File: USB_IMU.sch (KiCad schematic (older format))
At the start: 12 parts, among them U1301 LSM9DS1, U801 MCIMX7D7DVM10SC

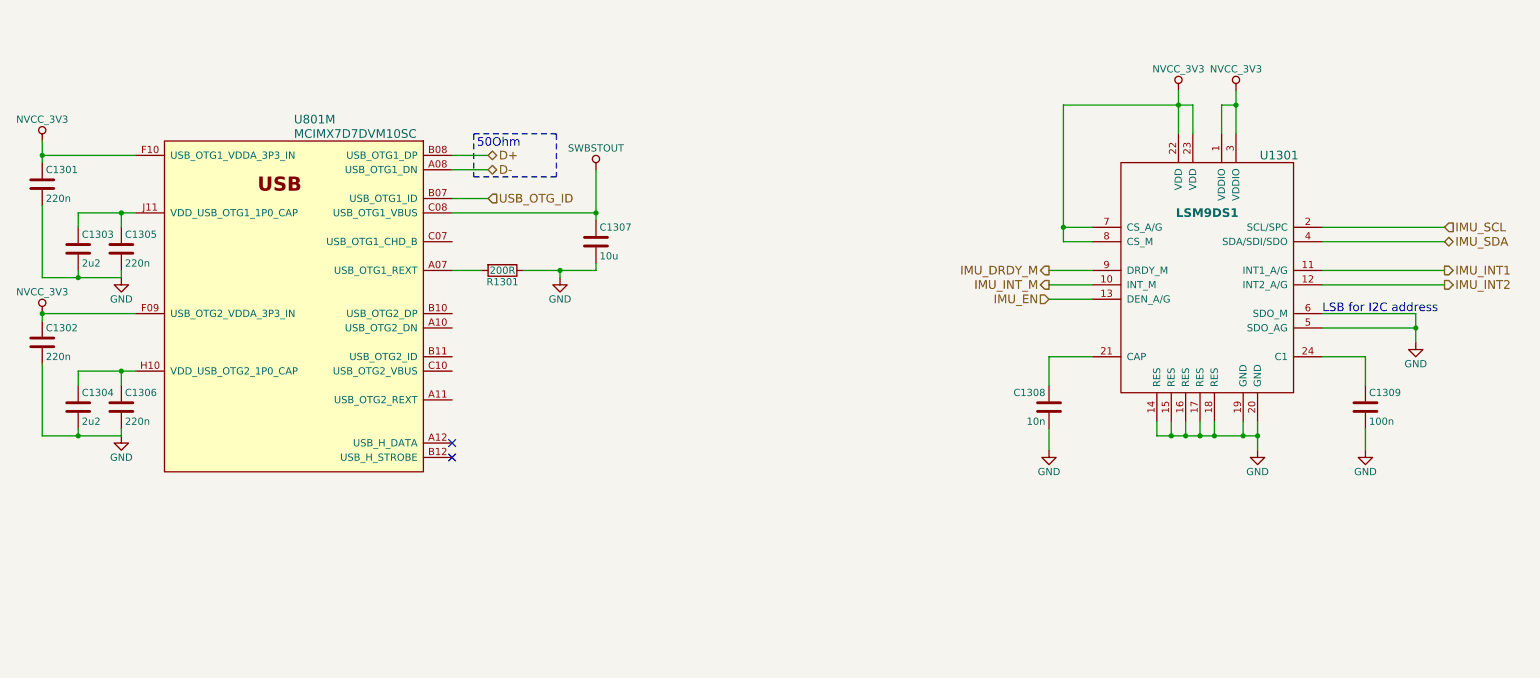
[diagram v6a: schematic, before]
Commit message: This branch moves from i.mx7 to STM32F4 CPU to be finished for Hackaday Prize 2017
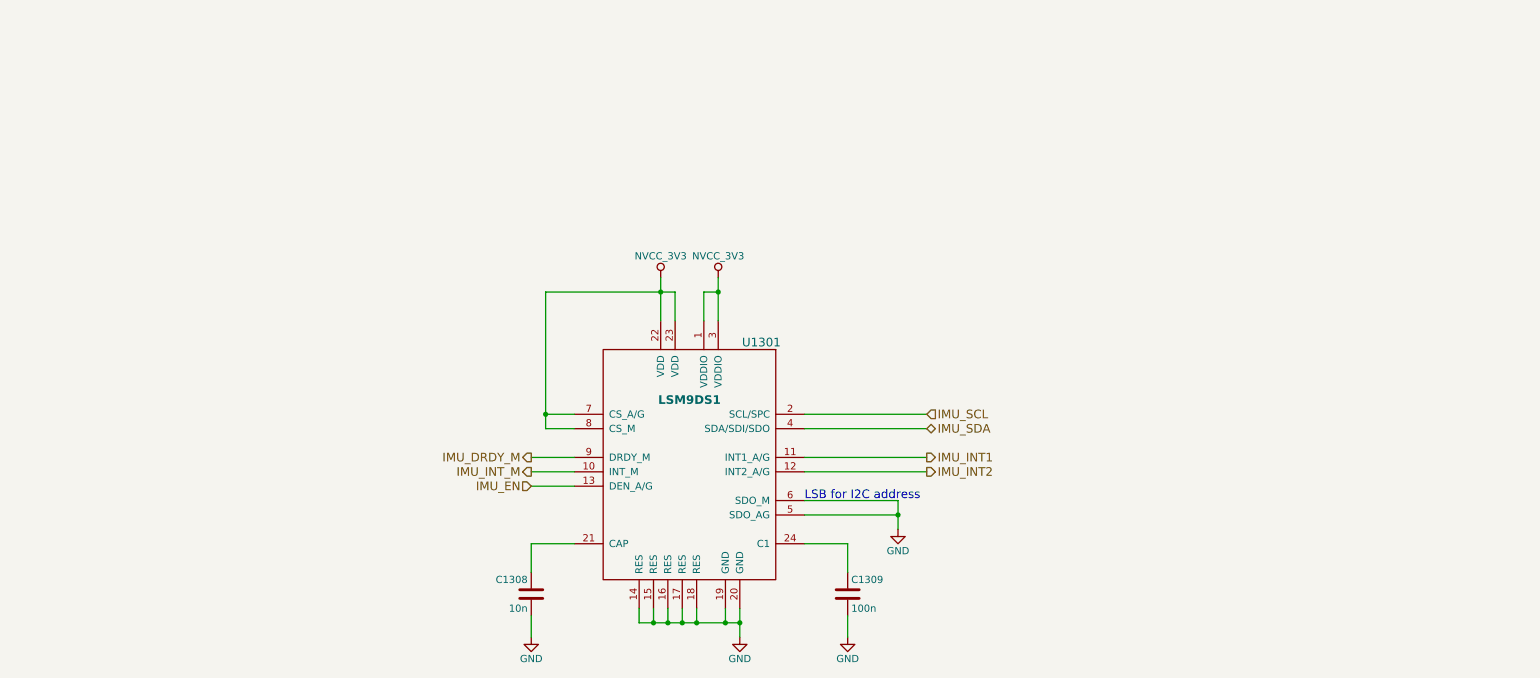
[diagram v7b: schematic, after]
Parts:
- removed C1301, C1302, C1305, C1306: 220n, Capacitors_SMD:C_0402, symbol C
- removed C1303, C1304: 2u2, Capacitors_SMD:C_0603, symbol C
- removed C1307: 10u, Capacitors_SMD:C_0603, symbol C
- removed R1301: 200R, Resistors_SMD:R_0402, symbol R
- removed U801: MCIMX7D7DVM10SC, NokiaRetroFit:BGA_541_075_19x19, symbol MCIMX7D7DVM10SC
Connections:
- no-connect marks 2 -> 0
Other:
- note removed: "50Ohm"
- moved on the sheet: C1308, C1309, U1301

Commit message: Modification for STM32 adaption
For the Hackaday Prize 2017 I decided to switch to STM32 as CPU

*Power system was modified to just contain the charge IC,
*Boost converter for high voltage peripherals
*Buck converter for 3V3 for CPU and switchable NVCC_3V3
   for peripherie

CPU signals are routed and pinmux is done in firmware folder.

SD-Card has 4bit Interface

WiFi module ESP8266 is connected via UART

Wolfson Ausio codec is connected via SAI

Two digital microphones for noise canceling

Rumble Motor driver

LCD is connected via it's own I2C interface
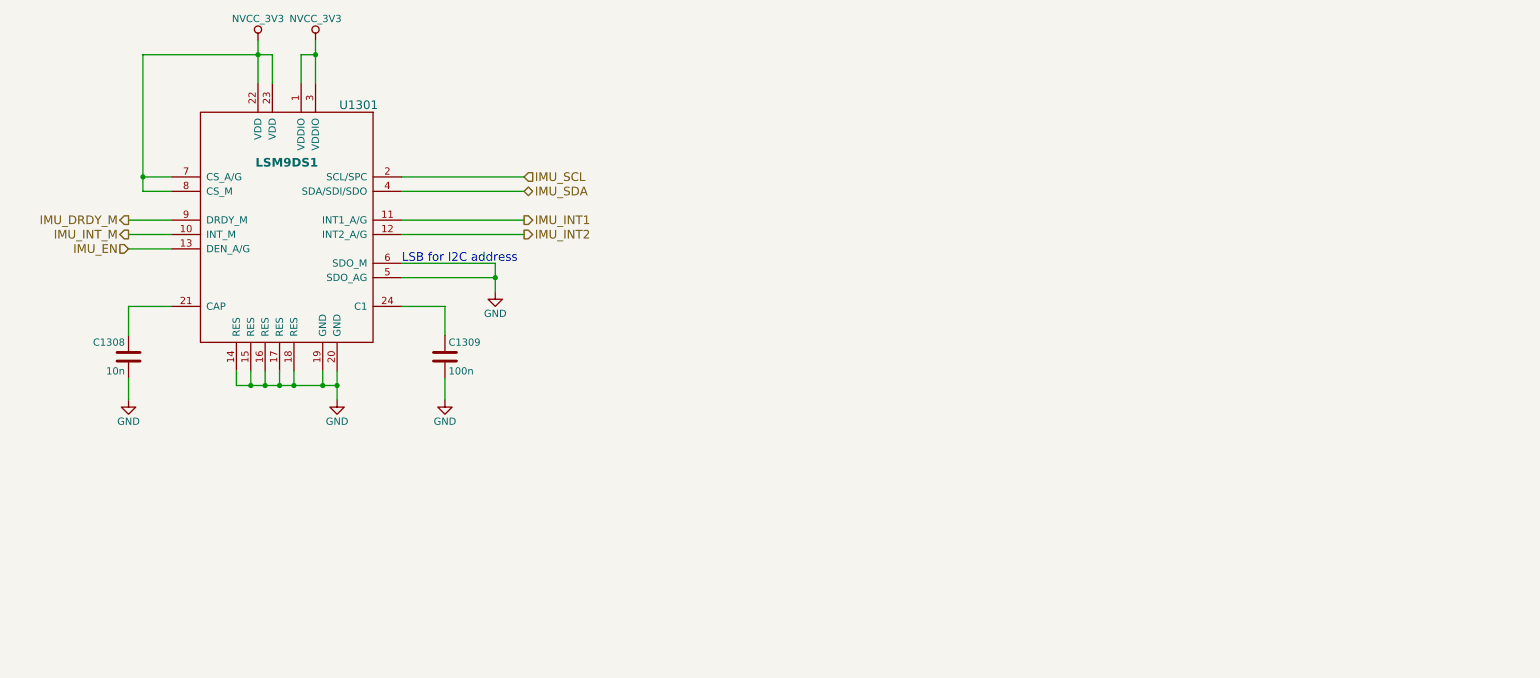
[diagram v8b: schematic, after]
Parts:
- C1308: footprint Capacitors_SMD:C_0603 -> Capacitors_SMD:C_0402_NoSilk
- C1309: footprint Capacitors_SMD:C_0402 -> Capacitors_SMD:C_0402_NoSilk
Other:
- moved on the sheet: C1308, C1309, U1301
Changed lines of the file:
@@
 EESchema Schematic File Version 2
-LIBS:3210retro-rescue
 LIBS:a7
 LIBS:ft232rl
@@
 LIBS:contrib
 LIBS:valves
-LIBS:stm32
+LIBS:tps62742
+LIBS:WM8994ECS
 LIBS:3210retro-cache
 EELAYER 26 0
 EELAYER END
-$Descr A3 16535 11693
+$Descr A4 11693 8268
 encoding utf-8
 Sheet 10 10
 Title "Nokia 3210 Retrofit"
-Date "2017-06-15"
-Rev "2"
-Comp ""
-Comment1 "Retrofitting board for Nokia 3210 mobile phone"
-Comment2 ""
+Date "2017-09-07"
+Rev "3"
+Comp "www.kurzschluss-blog.de"
+Comment1 "Retro fitting board for Nokia 3210 mobile phone"
+Comment2 "STM32 Version"
 Comment3 ""
 Comment4 ""
@@
 L NVCC_3V3 #PWR0310
 U 1 1 59430BB5
-P 8600 4200
+P 5800 2550
 AR Path="/5805F47D/594C5B6F/59430BB5" Ref="#PWR0310"  Part="1"
 AR Path="/59B32194/59430BB5" Ref="#PWR0310"  Part="1"
-F 0 "#PWR0310" H 8600 4050 50  0001 C CNN
-F 1 "NVCC_3V3" H 8600 4350 50  0000 C CNN
-F 2 "" H 8600 4200 50  0001 C CNN
-F 3 "" H 8600 4200 50  0001 C CNN
-	1    8600 4200
-	1    0    0    -1
-$EndComp
-Connection ~ 8600 4300
-Wire Wire Line
-	8500 4300 8600 4300
-Wire Wire Line
-	8500 4500 8500 4300
-Wire Wire Line
-	8600 4200 8600 4500
+F 0 "#PWR0310" H 5800 2400 50  0001 C CNN
+F 1 "NVCC_3V3" H 5800 2700 50  0000 C CNN
+F 2 "" H 5800 2550 50  0001 C CNN
+F 3 "" H 5800 2550 50  0001 C CNN
+	1    5800 2550
+	1    0    0    -1
+$EndComp
+Connection ~ 5800 2650
+Wire Wire Line
+	5700 2650 5800 2650
+Wire Wire Line
+	5700 2850 5700 2650
+Wire Wire Line
+	5800 2550 5800 2850
 $Comp
 L NVCC_3V3 #PWR0309
 U 1 1 59430571
-P 8200 4200
+P 5400 2550
 AR Path="/5805F47D/594C5B6F/59430571" Ref="#PWR0309"  Part="1"
 AR Path="/59B32194/59430571" Ref="#PWR0309"  Part="1"
-F 0 "#PWR0309" H 8200 4050 50  0001 C CNN
-F 1 "NVCC_3V3" H 8200 4350 50  0000 C CNN
-F 2 "" H 8200 4200 50  0001 C CNN
-F 3 "" H 8200 4200 50  0001 C CNN
-	1    8200 4200
-	1    0    0    -1
-$EndComp
-Wire Wire Line
-	7300 6700 7300 6550
+F 0 "#PWR0309" H 5400 2400 50  0001 C CNN
+F 1 "NVCC_3V3" H 5400 2700 50  0000 C CNN
+F 2 "" H 5400 2550 50  0001 C CNN
+F 3 "" H 5400 2550 50  0001 C CNN
+	1    5400 2550
+	1    0    0    -1
+$EndComp
+Wire Wire Line
+	4500 5050 4500 4900
 $Comp
 L GND #PWR0308
 U 1 1 594304CF
-P 7300 6700
+P 4500 5050
 AR Path="/5805F47D/594C5B6F/594304CF" Ref="#PWR0308"  Part="1"
 AR Path="/59B32194/594304CF" Ref="#PWR0308"  Part="1"
-F 0 "#PWR0308" H 7300 6450 50  0001 C CNN
-F 1 "GND" H 7300 6550 50  0000 C CNN
-F 2 "" H 7300 6700 50  0000 C CNN
-F 3 "" H 7300 6700 50  0000 C CNN
-	1    7300 6700
+F 0 "#PWR0308" H 4500 4800 50  0001 C CNN
+F 1 "GND" H 4500 4900 50  0000 C CNN
+F 2 "" H 4500 5050 50  0000 C CNN
+F 3 "" H 4500 5050 50  0000 C CNN
+	1    4500 5050
 	-1   0    0    -1
 $EndComp
 Wire Wire Line
-	7300 6050 7600 6050
-Wire Wire Line
-	7300 6250 7300 6050
+	4500 4400 4800 4400
+Wire Wire Line
+	4500 4600 4500 4400
 $Comp
 L C C1308
 U 1 1 594304C7
-P 7300 6400
+P 4500 4750
 AR Path="/5805F47D/594C5B6F/594304C7" Ref="C1308"  Part="1"
 AR Path="/59B32194/594304C7" Ref="C1308"  Part="1"
-F 0 "C1308" H 7325 6500 50  0000 L CNN
-F 1 "10n" H 7325 6300 50  0000 L CNN
-F 2 "Capacitors_SMD:C_0603" H 7338 6250 50  0001 C CNN
-F 3 "" H 7300 6400 50  0000 C CNN
-	1    7300 6400
+F 0 "C1308" H 4525 4850 50  0000 L CNN
+F 1 "10n" H 4525 4650 50  0000 L CNN
+F 2 "Capacitors_SMD:C_0402_NoSilk" H 4538 4600 50  0001 C CNN
+F 3 "" H 4500 4750 50  0000 C CNN
+	1    4500 4750
 	-1   0    0    -1
 $EndComp
 Wire Wire Line
-	9500 6700 9500 6550
+	6700 5050 6700 4900
 $Comp
 L GND #PWR0307
 U 1 1 594303C6
-P 9500 6700
+P 6700 5050
 AR Path="/5805F47D/594C5B6F/594303C6" Ref="#PWR0307"  Part="1"
 AR Path="/59B32194/594303C6" Ref="#PWR0307"  Part="1"
-F 0 "#PWR0307" H 9500 6450 50  0001 C CNN
-F 1 "GND" H 9500 6550 50  0000 C CNN
-F 2 "" H 9500 6700 50  0000 C CNN
-F 3 "" H 9500 6700 50  0000 C CNN
-	1    9500 6700
-	1    0    0    -1
-$EndComp
-Wire Wire Line
-	9500 6050 9200 6050
-Wire Wire Line
-	9500 6250 9500 6050
+F 0 "#PWR0307" H 6700 4800 50  0001 C CNN
+F 1 "GND" H 6700 4900 50  0000 C CNN
+F 2 "" H 6700 5050 50  0000 C CNN
+F 3 "" H 6700 5050 50  0000 C CNN
+	1    6700 5050
+	1    0    0    -1
+$EndComp
+Wire Wire Line
+	6700 4400 6400 4400
+Wire Wire Line
+	6700 4600 6700 4400
 $Comp
 L C C1309
 U 1 1 59430293
-P 9500 6400
+P 6700 4750
 AR Path="/5805F47D/594C5B6F/59430293" Ref="C1309"  Part="1"
 AR Path="/59B32194/59430293" Ref="C1309"  Part="1"
-F 0 "C1309" H 9525 6500 50  0000 L CNN
-F 1 "100n" H 9525 6300 50  0000 L CNN
-F 2 "Capacitors_SMD:C_0402" H 9538 6250 50  0001 C CNN
-F 3 "" H 9500 6400 50  0000 C CNN
-	1    9500 6400
-	1    0    0    -1
-$EndComp
-Text HLabel 7300 5650 0    60   Input ~ 0
+F 0 "C1309" H 6725 4850 50  0000 L CNN
+F 1 "100n" H 6725 4650 50  0000 L CNN
+F 2 "Capacitors_SMD:C_0402_NoSilk" H 6738 4600 50  0001 C CNN
+F 3 "" H 6700 4750 50  0000 C CNN
+	1    6700 4750
+	1    0    0    -1
+$EndComp
+Text HLabel 4500 4000 0    60   Input ~ 0
 IMU_EN
 Wire Wire Line
-	7600 5550 7300 5550
-Wire Wire Line
-	7300 5650 7600 5650
-Text HLabel 7300 5550 0    60   Output ~ 0
+	4800 3900 4500 3900
+Wire Wire Line
+	4500 4000 4800 4000
+Text HLabel 4500 3900 0    60   Output ~ 0
 IMU_INT_M
 Wire Wire Line
-	7300 5450 7600 5450
-Text HLabel 7300 5450 0    60   Output ~ 0
+	4500 3800 4800 3800
+Text HLabel 4500 3800 0    60   Output ~ 0
 IMU_DRDY_M
 $Comp
 L GND #PWR0306
 U 1 1 59430085
-P 9850 5950
+P 7050 4300
 AR Path="/5805F47D/594C5B6F/59430085" Ref="#PWR0306"  Part="1"
 AR Path="/59B32194/59430085" Ref="#PWR0306"  Part="1"
-F 0 "#PWR0306" H 9850 5700 50  0001 C CNN
-F 1 "GND" H 9850 5800 50  0000 C CNN
-F 2 "" H 9850 5950 50  0000 C CNN
-F 3 "" H 9850 5950 50  0000 C CNN
-	1    9850 5950
-	1    0    0    -1
-$EndComp
-Text Notes 9200 5750 0    60   ~ 0
+F 0 "#PWR0306" H 7050 4050 50  0001 C CNN
+F 1 "GND" H 7050 4150 50  0000 C CNN
+F 2 "" H 7050 4300 50  0000 C CNN
+F 3 "" H 7050 4300 50  0000 C CNN
+	1    7050 4300
+	1    0    0    -1
+$EndComp
+Text Notes 6400 4100 0    60   ~ 0
 LSB for I2C address
-Connection ~ 9850 5850
-Wire Wire Line
-	9200 5850 9850 5850
-Wire Wire Line
-	9850 5750 9850 5950
-Wire Wire Line
-	9200 5750 9850 5750
-Connection ~ 8750 6600
+Connection ~ 7050 4200
+Wire Wire Line
+	6400 4200 7050 4200
+Wire Wire Line
+	7050 4100 7050 4300
+Wire Wire Line
+	6400 4100 7050 4100
+Connection ~ 5950 4950
 $Comp
 L GND #PWR0305
 U 1 1 5942FEDE
-P 8750 6700
+P 5950 5050
 AR Path="/5805F47D/594C5B6F/5942FEDE" Ref="#PWR0305"  Part="1"
 AR Path="/59B32194/5942FEDE" Ref="#PWR0305"  Part="1"
-F 0 "#PWR0305" H 8750 6450 50  0001 C CNN
-F 1 "GND" H 8750 6550 50  0000 C CNN
-F 2 "" H 8750 6700 50  0000 C CNN
-F 3 "" H 8750 6700 50  0000 C CNN
-	1    8750 6700
-	1    0    0    -1
-$EndComp
-Connection ~ 8150 6600
-Wire Wire Line
-	8150 6500 8150 6600
-Connection ~ 8250 6600
-Wire Wire Line
-	8250 6500 8250 6600
-Connection ~ 8350 6600
-Wire Wire Line
-	8350 6500 8350 6600
-Connection ~ 8450 6600
-Wire Wire Line
-	8450 6500 8450 6600
-Connection ~ 8650 6600
-Wire Wire Line
-	8650 6500 8650 6600
-Wire Wire Line
-	8750 6500 8750 6700
-Wire Wire Line
-	8050 6600 8750 6600
-Wire Wire Line
-	8050 6500 8050 6600
-Wire Wire Line
-	9200 5450 10050 5450
-Wire Wire Line
-	10050 5550 9200 5550
-Text HLabel 10050 5550 2    60   Output ~ 0
+F 0 "#PWR0305" H 5950 4800 50  0001 C CNN
+F 1 "GND" H 5950 4900 50  0000 C CNN
+F 2 "" H 5950 5050 50  0000 C CNN
+F 3 "" H 5950 5050 50  0000 C CNN
+	1    5950 5050
+	1    0    0    -1
+$EndComp
+Connection ~ 5350 4950
+Wire Wire Line
+	5350 4850 5350 4950
+Connection ~ 5450 4950
+Wire Wire Line
+	5450 4850 5450 4950
+Connection ~ 5550 4950
+Wire Wire Line
+	5550 4850 5550 4950
+Connection ~ 5650 4950
+Wire Wire Line
+	5650 4850 5650 4950
+Connection ~ 5850 4950
+Wire Wire Line
+	5850 4850 5850 4950
+Wire Wire Line
+	5950 4850 5950 5050
+Wire Wire Line
+	5250 4950 5950 4950
+Wire Wire Line
+	5250 4850 5250 4950
+Wire Wire Line
+	6400 3800 7250 3800
+Wire Wire Line
+	7250 3900 6400 3900
+Text HLabel 7250 3900 2    60   Output ~ 0
 IMU_INT2
-Text HLabel 10050 5450 2    60   Output ~ 0
+Text HLabel 7250 3800 2    60   Output ~ 0
 IMU_INT1
 Wire Wire Line
-	10050 5250 9200 5250
-Wire Wire Line
-	9200 5150 10050 5150
-Connection ~ 8200 4300
-Wire Wire Line
-	8200 4200 8200 4500
-Connection ~ 7400 5150
-Wire Wire Line
-	7600 5150 7400 5150
-Wire Wire Line
-	7400 5250 7600 5250
-Wire Wire Line
-	7400 4300 7400 5250
-Wire Wire Line
-	7400 4300 8300 4300
-Wire Wire Line
-	8300 4300 8300 4500
+	7250 3600 6400 3600
+Wire Wire Line
+	6400 3500 7250 3500
+Connection ~ 5400 2650
+Wire Wire Line
+	5400 2550 5400 2850
+Connection ~ 4600 3500
+Wire Wire Line
+	4800 3500 4600 3500
+Wire Wire Line
+	4600 3600 4800 3600
+Wire Wire Line
+	4600 2650 4600 3600
+Wire Wire Line
+	4600 2650 5500 2650
+Wire Wire Line
+	5500 2650 5500 2850
 $Comp
 L LSM9DS1 U1301
 U 1 1 5942F947
-P 8400 5650
+P 5600 4000
 AR Path="/5805F47D/594C5B6F/5942F947" Ref="U1301"  Part="1"
 AR Path="/59B32194/5942F947" Ref="U1301"  Part="1"
-F 0 "U1301" H 8900 6650 60  0000 C CNN
-F 1 "LSM9DS1" H 8400 6250 60  0000 C CNB
-F 2 "NokiaRetroFit:LSM9DS1" H 8400 5650 60  0001 C CNN
-F 3 "" H 8400 5650 60  0001 C CNN
-	1    8400 5650
-	1    0    0    -1
-$EndComp
-Text HLabel 10050 5150 2    60   Input ~ 0
+F 0 "U1301" H 6100 5000 60  0000 C CNN
+F 1 "LSM9DS1" H 5600 4600 60  0000 C CNB
+F 2 "NokiaRetroFit:LSM9DS1" H 5600 4000 60  0001 C CNN
+F 3 "" H 5600 4000 60  0001 C CNN
+	1    5600 4000
+	1    0    0    -1
+$EndComp
+Text HLabel 7250 3500 2    60   Input ~ 0
 IMU_SCL
-Text HLabel 10050 5250 2    60   BiDi ~ 0
+Text HLabel 7250 3600 2    60   BiDi ~ 0
 IMU_SDA
 $EndSCHEMATC
